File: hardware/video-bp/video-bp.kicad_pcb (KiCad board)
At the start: 2 copper layers, 99.9 x 61.9 mm, 11 parts, among them J1 GPIO9, J2 GPIO8, J3 GPIO5, J4 GPIO4

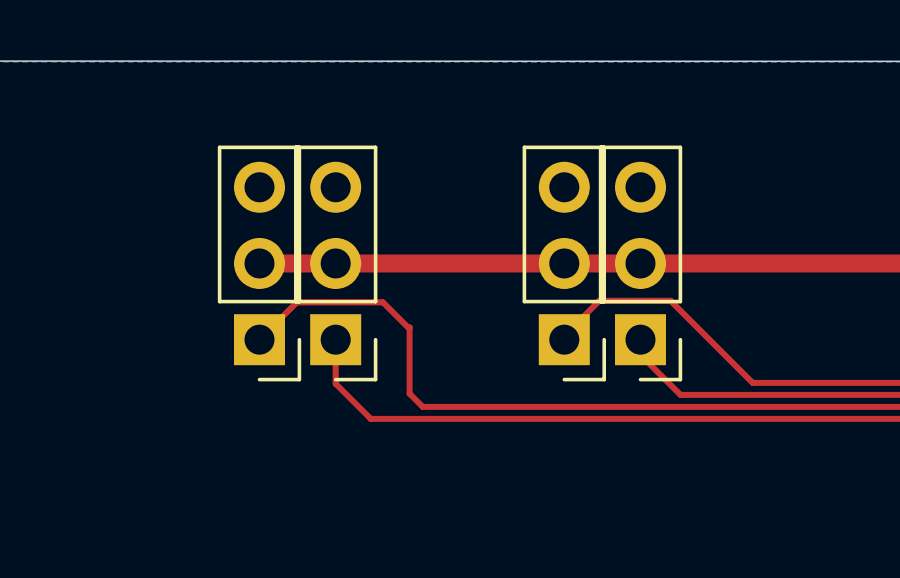
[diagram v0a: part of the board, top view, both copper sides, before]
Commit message: Rev 1.1: - Update to latest KiCad - Fixed short in servo board - Updates to right-angle diag connector on servo boards - Fixed microproc footprint on diag board - Flipped I2C connector to top of diag board - Pass all ERC and DRC checks, add exclusions
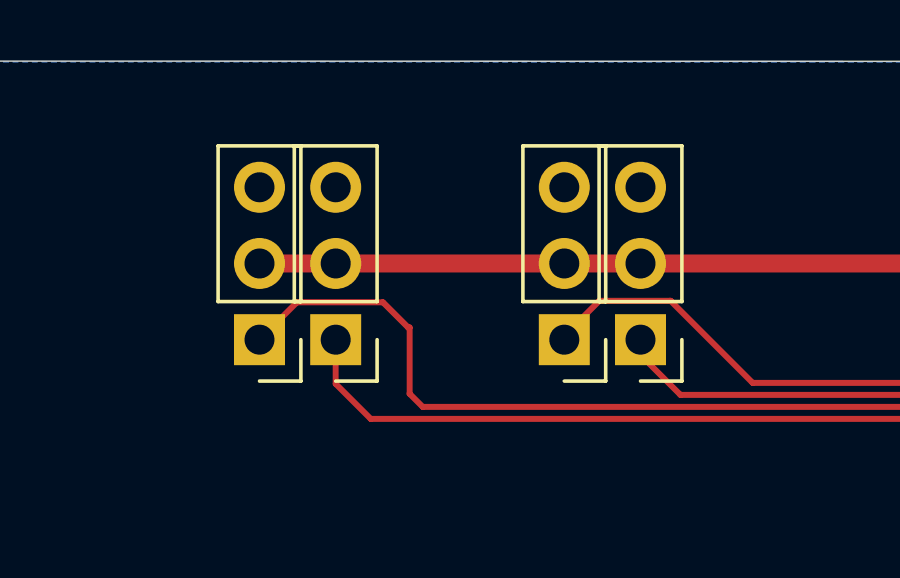
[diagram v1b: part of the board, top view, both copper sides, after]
